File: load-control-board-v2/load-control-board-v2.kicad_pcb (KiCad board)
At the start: 4 copper layers, 100 x 80 mm, 96 parts, among them CN1 3511232BMRS0BNA2, CN2 BTC22M4NBB4SCM, CN3 BTC22M4NBB4SCM, Q1 AO3400A, Q2 AO3400A, Q3 IRFP7530PBF, U1 LM317_SOT-223, U10 OPA188xxDBV, U11 OPA188xxDBV, U12 INA186A1IDCKR, U2 74AHC1G04, U22 TL081HIDBVR, U3 LM317_SOT-223, U5 REF5025AD, U6 SN74LVC1G123DCUR_C352969, U7 ALERT_COMP_OUT, U8 OPA188xxDBV

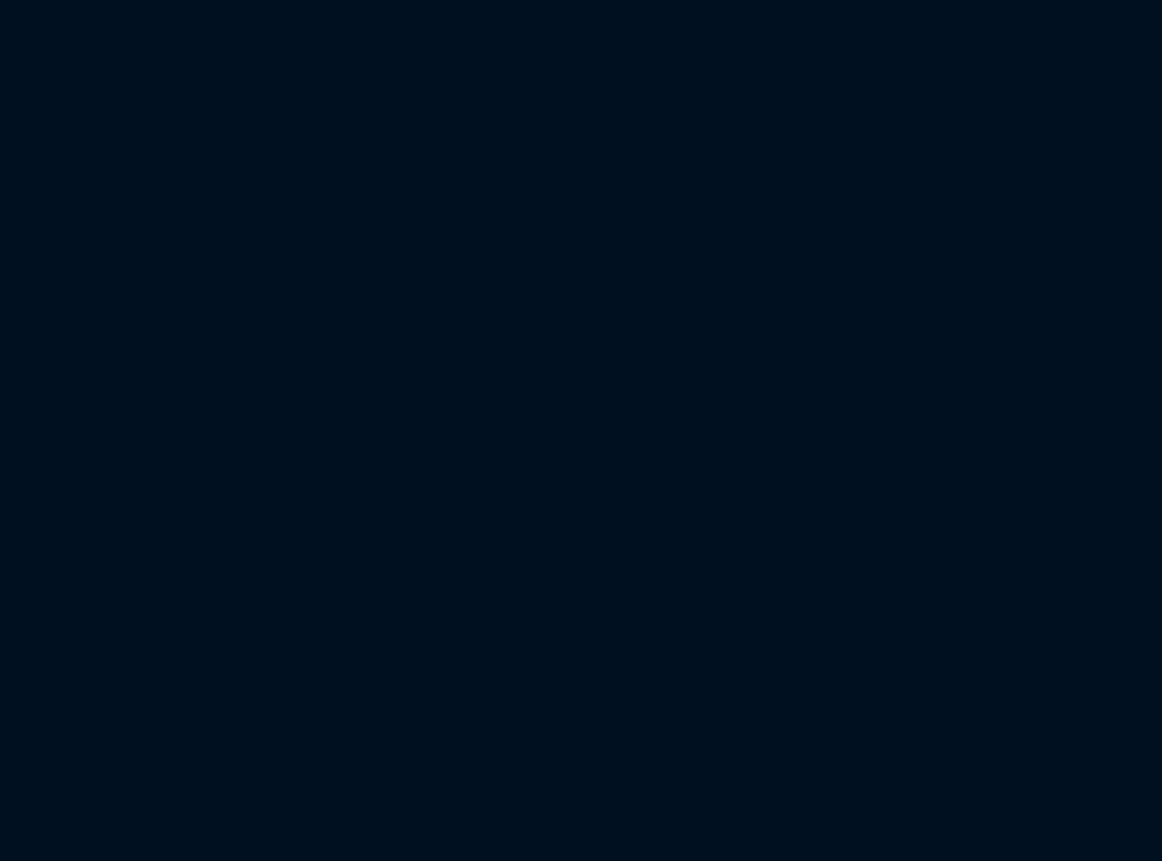
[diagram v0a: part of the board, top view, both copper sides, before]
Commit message: Add 2011 heat sink
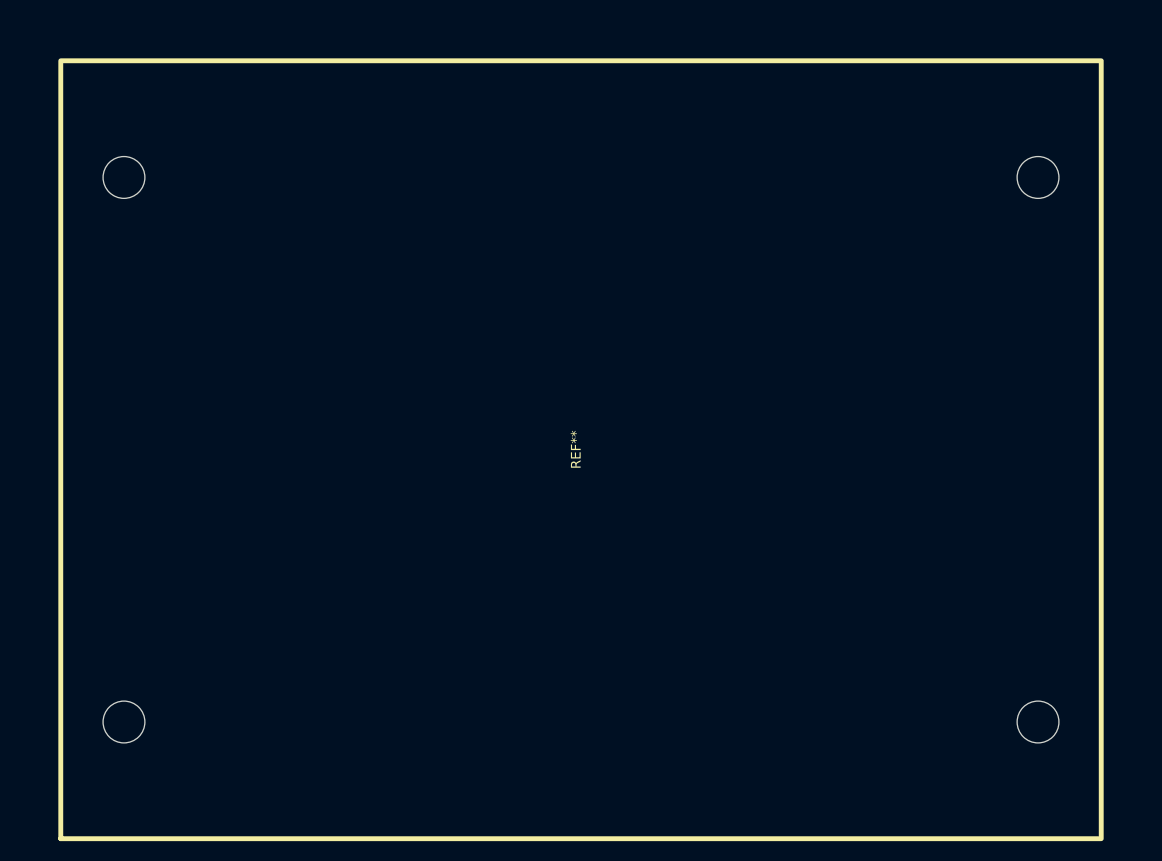
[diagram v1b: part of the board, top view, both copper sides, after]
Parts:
- added REF**: HEAT_SINK_2011, programmable-load-library:HEAT_SINK_2011, F.Cu at (89.7, 181.0)
